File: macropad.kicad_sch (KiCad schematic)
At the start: 14 parts, among them J1 Conn_01x03_Pin, J2 Conn_01x02_Pin, SW1 SW_Push, SW2 SW_Push, SW3 SW_Push, U1 XIAO-RP2040-DIP

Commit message: Rewire power LED to 3V
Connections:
- net Power: now also U1.12 (3V3); no longer U1.14 (VBUS)
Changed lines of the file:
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@@
 	)
 	(no_connect
-		(at 115.57 83.82)
+		(at 115.57 76.2)
 	)
 	(no_connect
@@
 	(global_label "Power"
 		(shape input)
-		(at 115.57 76.2 0)
+		(at 115.57 83.82 0)
 		(fields_autoplaced yes)
 		(effects
@@
 		)
 		(property "Intersheetrefs" "${INTERSHEET_REFS}"
-			(at 124.1795 76.2 0)
+			(at 124.1795 83.82 0)
 			(effects
 				(font

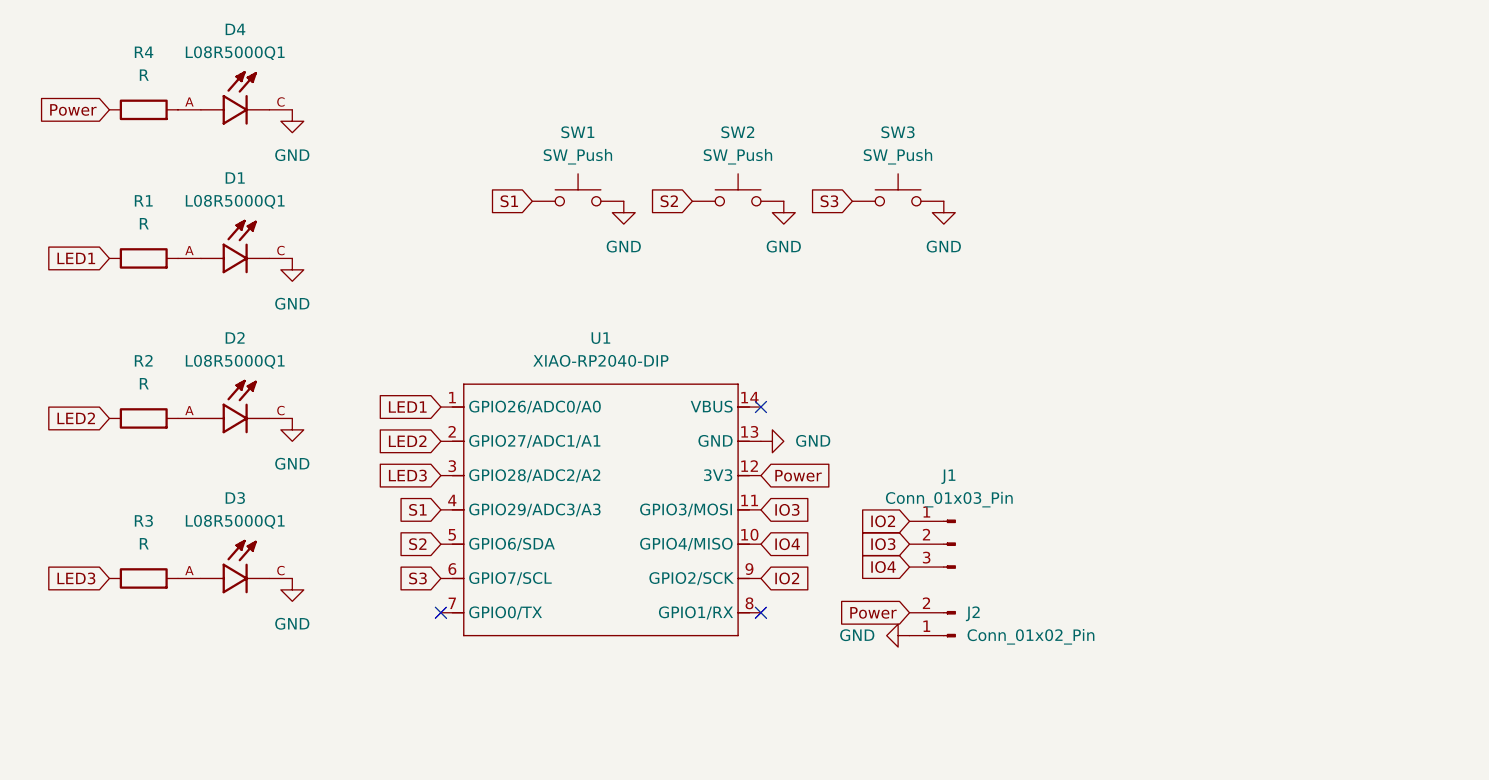
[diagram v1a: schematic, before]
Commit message: Add brightness adjust and edit firmware
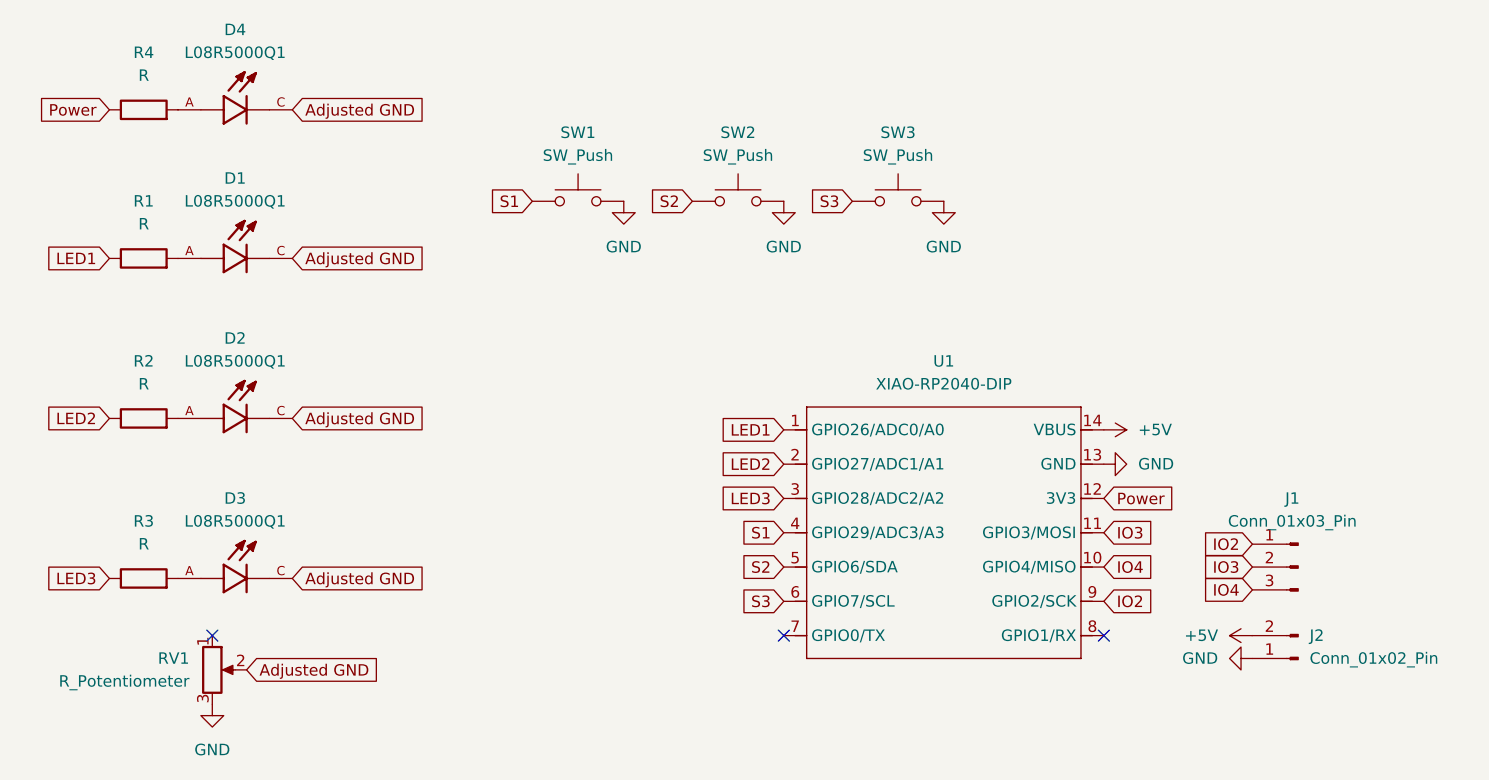
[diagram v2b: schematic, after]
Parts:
- added RV1: R_Potentiometer, Potentiometer_THT:Potentiometer_Vishay_T73YP_Vertical, symbol Device:R_Potentiometer
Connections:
- net GND: now also RV1.3; no longer D1.C, D2.C, D3.C, D4.C
- net Power: no longer J2.2 (Pin_2)
- net +5V: now reaches U1.14 (VBUS)
- net +5V: now also J2.2 (Pin_2)
- new net Adjusted GND: D1.C, D2.C, D3.C, D4.C, RV1.2
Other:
- moved on the sheet: J1, J2, U1
